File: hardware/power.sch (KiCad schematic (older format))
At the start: 42 parts, among them P1 CONN_01X02, Q1 Q_NMOS_GDS, SW1 SPST, U7 LT3471, U8 PDM1-S

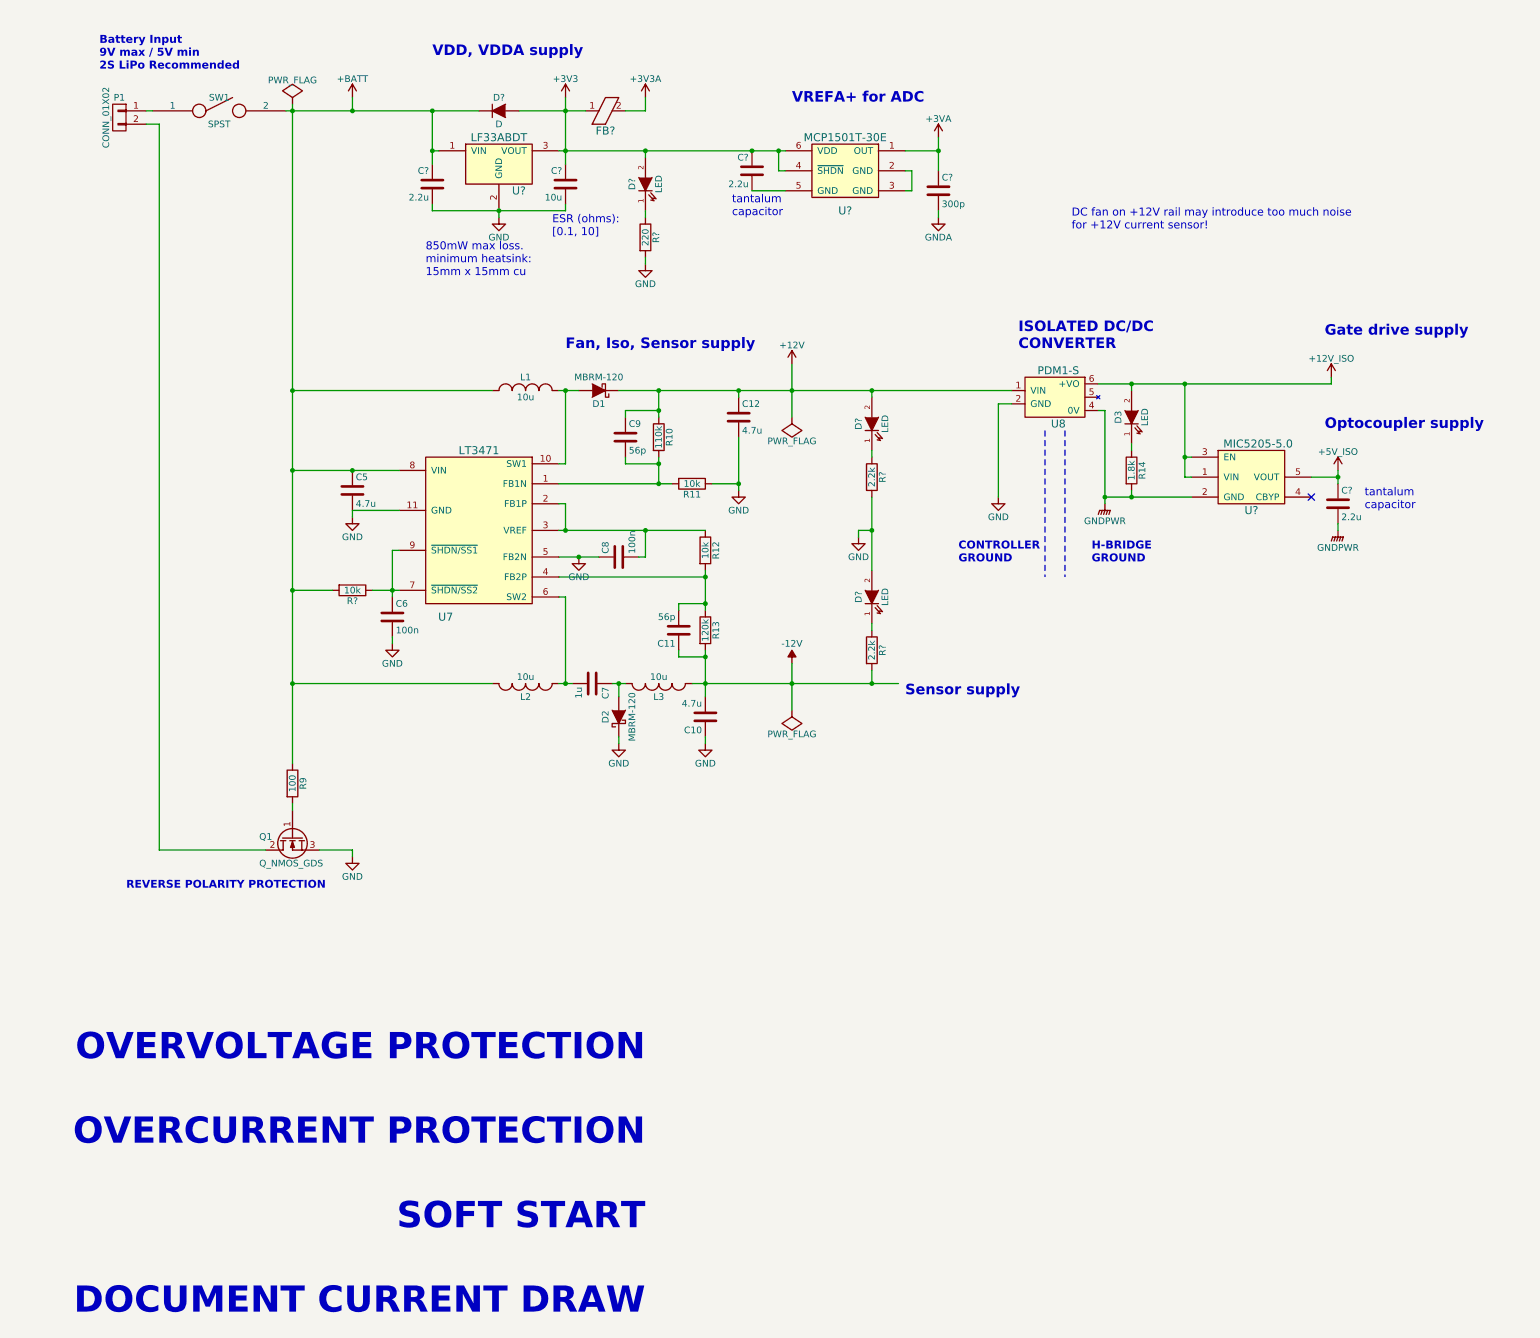
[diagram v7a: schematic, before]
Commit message: Finish MCU HW draft 1; adjust sensors for 3v ref
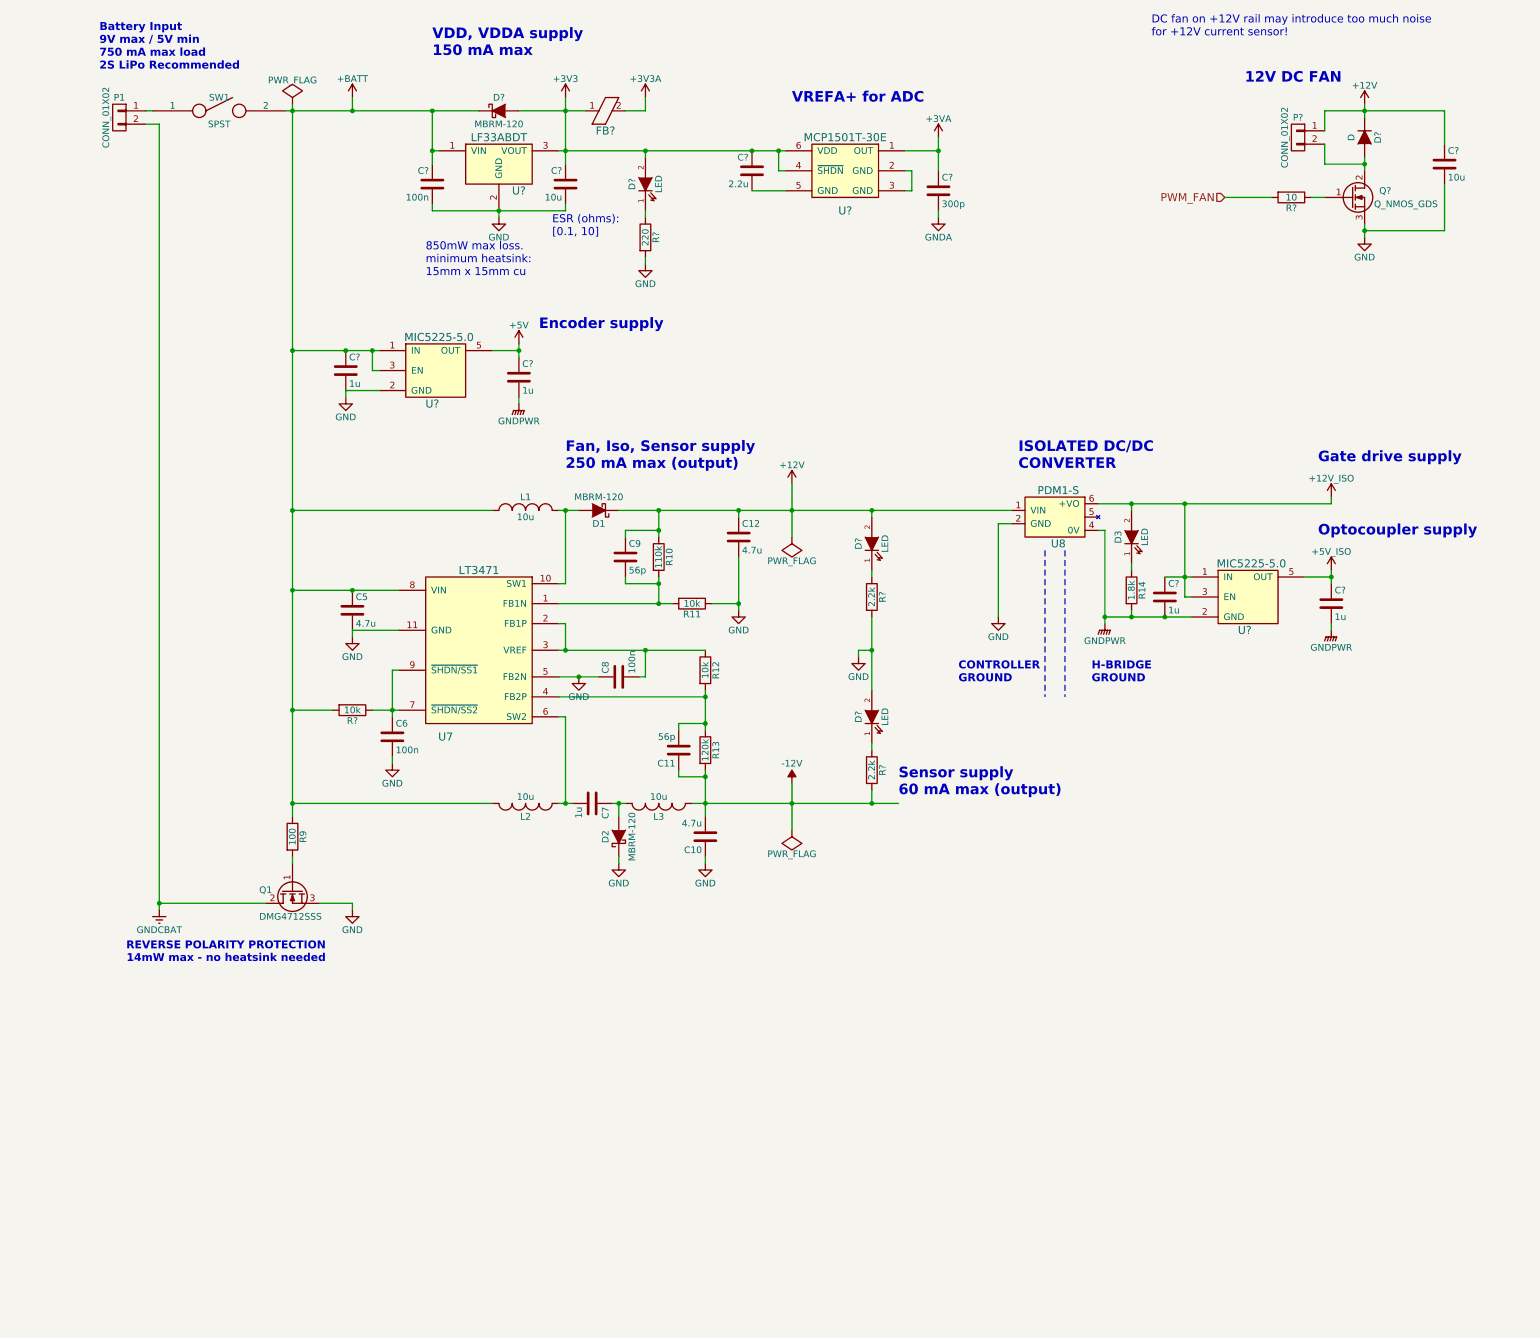
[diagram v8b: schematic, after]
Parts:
- removed D?: D, symbol D
- removed U?: MIC5205-5.0, symbol MIC5205-5.0
- added C? (x3): 1u, symbol C
- added C?: 10u, symbol C
- added D?: MBRM-120, Diodes_SMD:SOD-123, symbol D_Schottky
- added D?: D, symbol D
- added P?: CONN_01X02, symbol CONN_01X02
- added Q?: Q_NMOS_GDS, symbol Q_NMOS_GDS
- added R?: 10, symbol R
- added U? (x2): MIC5225-5.0, symbol MIC5225-5.0
- C?: value 2.2u -> 100n
- C?: value 2.2u -> 1u
- Q1: value Q_NMOS_GDS -> DMG4712SSS
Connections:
- net +12V: now also C?.1, D?.1 (K), P?.1 (P1)
- net +12V_ISO: now also C?.1, U?.1 (IN), U?.3 (EN)
- net +3V3: now also D?.2 (A)
- net +5V_ISO: now also U?.5 (OUT)
- net +BATT: now also C?.1, D?.1 (K), U?.1 (IN), U?.3 (EN)
- net GND: now also C?.2, C?.2, Q?.3 (S), U?.2 (GND)
- net GNDPWR: now also C?.2, C?.2, U?.2 (GND)
- net GNDCBAT: now reaches P1.2 (P2), Q1.2 (D)
- new net: Q?.1 (G), R?.1
- new net: D?.2 (A), P?.2 (P2), Q?.2 (D)
- new net +5V: C?.1, U?.5 (OUT)
- new net PWM_FAN: R?.2
- no-connect marks 1 -> 0
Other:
- note added: "12V DC FAN"
- note added: "Battery Input\n9V max / 5V min\n750 mA max load\n2S LiPo Recommended"
- note added: "Encoder supply"
- note added: "Fan, Iso, Sensor supply\n250 mA max (output)"
- note added: "REVERSE POLARITY PROTECTION\n14mW max - no heatsink needed"
- note added: "Sensor supply\n60 mA max (output)"
- note added: "VDD, VDDA supply\n150 mA max"
- note removed: "Battery Input\n9V max / 5V min\n2S LiPo Recommended"
- note removed: "Fan, Iso, Sensor supply"
- note removed: "OVERVOLTAGE PROTECTION\n\nOVERCURRENT PROTECTION\n\nSOFT START\n\nDOCUMENT CURRENT DRAW"
- note removed: "REVERSE POLARITY PROTECTION"
- note removed: "Sensor supply"
- note removed: "VDD, VDDA supply"
- note removed: "tantalum\ncapacitor"
- moved on the sheet: C10, C11, C12, C5, C6, C7, C8, C9, C?, D1, D2, D3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
